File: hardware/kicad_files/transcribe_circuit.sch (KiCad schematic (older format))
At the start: 17 parts, among them J1 RS232_SERIAL, J2 MIDI_IN, J3 MIDI_OUT, U1 ProMicro, U2 MAX232, U3 6N137, U4 usbHostMini, U5 LM1117-3.3

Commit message: works with and without usb-device connected now
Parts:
- added J?: RS232_DSUB, symbol Connector:DB9_Female_MountingHoles
- C1, C2, C3, C4: footprint (none) -> Capacitor_THT:C_Axial_L3.8mm_D2.6mm_P7.50mm_Horizontal
- D1: footprint (none) -> Diode_THT:D_A-405_P7.62mm_Horizontal
- J1, J2, J3: footprint (none) -> Connector_Audio:Jack_3.5mm_CUI_SJ1-3533NG_Horizontal_CircularHoles
- R1, R2, R3, R4: footprint (none) -> Resistor_THT:R_Axial_DIN0207_L6.3mm_D2.5mm_P10.16mm_Horizontal
- U2: footprint (none) -> Package_DIP:DIP-16_W7.62mm
- U5: footprint (none) -> Package_TO_SOT_THT:TO-220-3_Horizontal_TabDown
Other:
- note added: "A. micro-controller"
- note added: "B. rs232 serial"
- note added: "C. midi serial"
- note added: "D. usb-host shield"
- note removed: "micro-controller"
- note removed: "midi serial"
- note removed: "rs232 serial"
- note removed: "usb-host shield"
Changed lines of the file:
@@
 F 0 "U1" H 2200 3537 60  0000 C CNN
 F 1 "ProMicro" H 2200 3431 60  0000 C CNN
-F 2 "" H 2300 1450 60  0000 C CNN
+F 2 "" H 2300 1450 60  0001 C CNN
 F 3 "" H 2300 1450 60  0000 C CNN
 	1    2200 2500
@@
 F 0 "U2" H 4750 4625 50  0000 C CNN
 F 1 "MAX232" H 4850 4525 50  0000 C CNN
-F 2 "" H 5250 2300 50  0001 L CNN
+F 2 "Package_DIP:DIP-16_W7.62mm" H 5250 2300 50  0001 L CNN
 F 3 "http://www.ti.com/lit/ds/symlink/max232.pdf" H 5200 3450 50  0001 C CNN
 	1    5200 3350
@@
 F 0 "U4" H 2575 7437 60  0000 C CNN
 F 1 "usbHostMini" H 2575 7331 60  0000 C CNN
-F 2 "" H 2675 5350 60  0000 C CNN
+F 2 "" H 2675 5350 60  0001 C CNN
 F 3 "" H 2675 5350 60  0000 C CNN
 	1    2575 6400
@@
 $EndComp
 Text Notes 875  950  0    118  ~ 0
-micro-controller
+A. micro-controller
 Text Notes 4275 975  0    118  ~ 0
-rs232 serial
+B. rs232 serial
 Text Notes 1000 4525 0    118  ~ 0
-usb-host shield
+D. usb-host shield
 Text Notes 7450 1025 0    118  ~ 0
-midi serial
+C. midi serial
 $Comp
 L Isolator:6N137 U3
@@
 F 0 "R1" V 8450 2225 50  0000 C CNN
 F 1 "220" V 8550 2225 50  0000 C CNN
-F 2 "" V 8480 2225 50  0001 C CNN
+F 2 "Resistor_THT:R_Axial_DIN0207_L6.3mm_D2.5mm_P10.16mm_Horizontal" V 8480 2225 50  0001 C CNN
 F 3 "~" H 8550 2225 50  0001 C CNN
 	1    8550 2225
@@
 F 0 "R2" V 9950 2125 50  0000 C CNN
 F 1 "10k" V 10050 2125 50  0000 C CNN
-F 2 "" V 9980 2125 50  0001 C CNN
+F 2 "Resistor_THT:R_Axial_DIN0207_L6.3mm_D2.5mm_P10.16mm_Horizontal" V 9980 2125 50  0001 C CNN
 F 3 "~" H 10050 2125 50  0001 C CNN
 	1    10050 2125
@@
 F 0 "D1" V 8754 2454 50  0000 L CNN
 F 1 "1N4148" H 8700 2275 50  0000 L CNN
-F 2 "" H 8800 2375 50  0001 C CNN
+F 2 "Diode_THT:D_A-405_P7.62mm_Horizontal" H 8800 2375 50  0001 C CNN
 F 3 "~" H 8800 2375 50  0001 C CNN
 	1    8800 2375
@@
 F 0 "J2" H 7932 1975 50  0000 C CNN
 F 1 "MIDI_IN" H 7932 1884 50  0000 C CNN
-F 2 "" H 7950 1650 50  0001 C CNN
+F 2 "Connector_Audio:Jack_3.5mm_CUI_SJ1-3533NG_Horizontal_CircularHoles" H 7950 1650 50  0001 C CNN
 F 3 "~" H 7950 1650 50  0001 C CNN
 	1    7950 1650
@@
 F 0 "J3" H 8007 4525 50  0000 C CNN
 F 1 "MIDI_OUT" H 8007 4434 50  0000 C CNN
-F 2 "" H 8025 4200 50  0001 C CNN
+F 2 "Connector_Audio:Jack_3.5mm_CUI_SJ1-3533NG_Horizontal_CircularHoles" H 8025 4200 50  0001 C CNN
 F 3 "~" H 8025 4200 50  0001 C CNN
 	1    8025 4200
@@
 F 0 "R3" V 9975 4200 50  0000 C CNN
 F 1 "220" V 10075 4200 50  0000 C CNN
-F 2 "" V 10005 4200 50  0001 C CNN
+F 2 "Resistor_THT:R_Axial_DIN0207_L6.3mm_D2.5mm_P10.16mm_Horizontal" V 10005 4200 50  0001 C CNN
 F 3 "~" H 10075 4200 50  0001 C CNN
 	1    10075 4200
@@
 F 0 "R4" V 9975 4425 50  0000 C CNN
 F 1 "220" V 10075 4425 50  0000 C CNN
-F 2 "" V 10005 4425 50  0001 C CNN
+F 2 "Resistor_THT:R_Axial_DIN0207_L6.3mm_D2.5mm_P10.16mm_Horizontal" V 10005 4425 50  0001 C CNN
 F 3 "~" H 10075 4425 50  0001 C CNN
 	1    10075 4425
@@
 F 0 "C1" H 4265 2646 50  0000 L CNN
 F 1 "0.1u" H 4265 2555 50  0000 L CNN
-F 2 "" H 4188 2450 50  0001 C CNN
+F 2 "Capacitor_THT:C_Axial_L3.8mm_D2.6mm_P7.50mm_Horizontal" H 4188 2450 50  0001 C CNN
 F 3 "~" H 4150 2600 50  0001 C CNN
 	1    4150 2600
@@
 F 0 "C2" H 6365 2646 50  0000 L CNN
 F 1 "0.1u" H 6365 2555 50  0000 L CNN
-F 2 "" H 6288 2450 50  0001 C CNN
+F 2 "Capacitor_THT:C_Axial_L3.8mm_D2.6mm_P7.50mm_Horizontal" H 6288 2450 50  0001 C CNN
 F 3 "~" H 6250 2600 50  0001 C CNN
 	1    6250 2600
@@
 F 0 "C3" V 6000 2950 50  0000 C CNN
 F 1 "0.1u" V 6300 2950 50  0000 C CNN
-F 2 "" H 6188 2800 50  0001 C CNN
+F 2 "Capacitor_THT:C_Axial_L3.8mm_D2.6mm_P7.50mm_Horizontal" H 6188 2800 50  0001 C CNN
 F 3 "~" H 6150 2950 50  0001 C CNN
 	1    6150 2950
@@
 F 0 "C4" V 6150 3250 50  0000 C CNN
 F 1 "0.1u" V 6450 3250 50  0000 C CNN
-F 2 "" H 6338 3100 50  0001 C CNN
+F 2 "Capacitor_THT:C_Axial_L3.8mm_D2.6mm_P7.50mm_Horizontal" H 6338 3100 50  0001 C CNN
 F 3 "~" H 6300 3250 50  0001 C CNN
 	1    6300 3250
@@
 F 0 "J1" H 4132 1900 50  0000 C CNN
 F 1 "RS232_SERIAL" H 4025 1800 50  0000 C CNN
-F 2 "" H 4150 1575 50  0001 C CNN
+F 2 "Connector_Audio:Jack_3.5mm_CUI_SJ1-3533NG_Horizontal_CircularHoles" H 4150 1575 50  0001 C CNN
 F 3 "~" H 4150 1575 50  0001 C CNN
 	1    4150 1575
@@
 F 0 "U5" H 1300 5267 50  0000 C CNN
 F 1 "LM1117-3.3" H 1300 5176 50  0000 C CNN
-F 2 "" H 1300 5025 50  0001 C CNN
+F 2 "Package_TO_SOT_THT:TO-220-3_Horizontal_TabDown" H 1300 5025 50  0001 C CNN
 F 3 "http://www.ti.com/lit/ds/symlink/lm1117.pdf" H 1300 5025 50  0001 C CNN
 	1    1300 5025
@@
 Wire Wire Line
 	2900 1950 2950 1950
+$Comp
+L Connector:DB9_Female_MountingHoles J?
+U 1 1 5E3595C7
+P 5925 1575
+F 0 "J?" H 6105 1577 50  0000 L CNN
+F 1 "RS232_DSUB" H 6105 1486 50  0000 L CNN
+F 2 "" H 5925 1575 50  0001 C CNN
+F 3 " ~" H 5925 1575 50  0001 C CNN
+	1    5925 1575
+	1    0    0    -1
+$EndComp
 $EndSCHEMATC

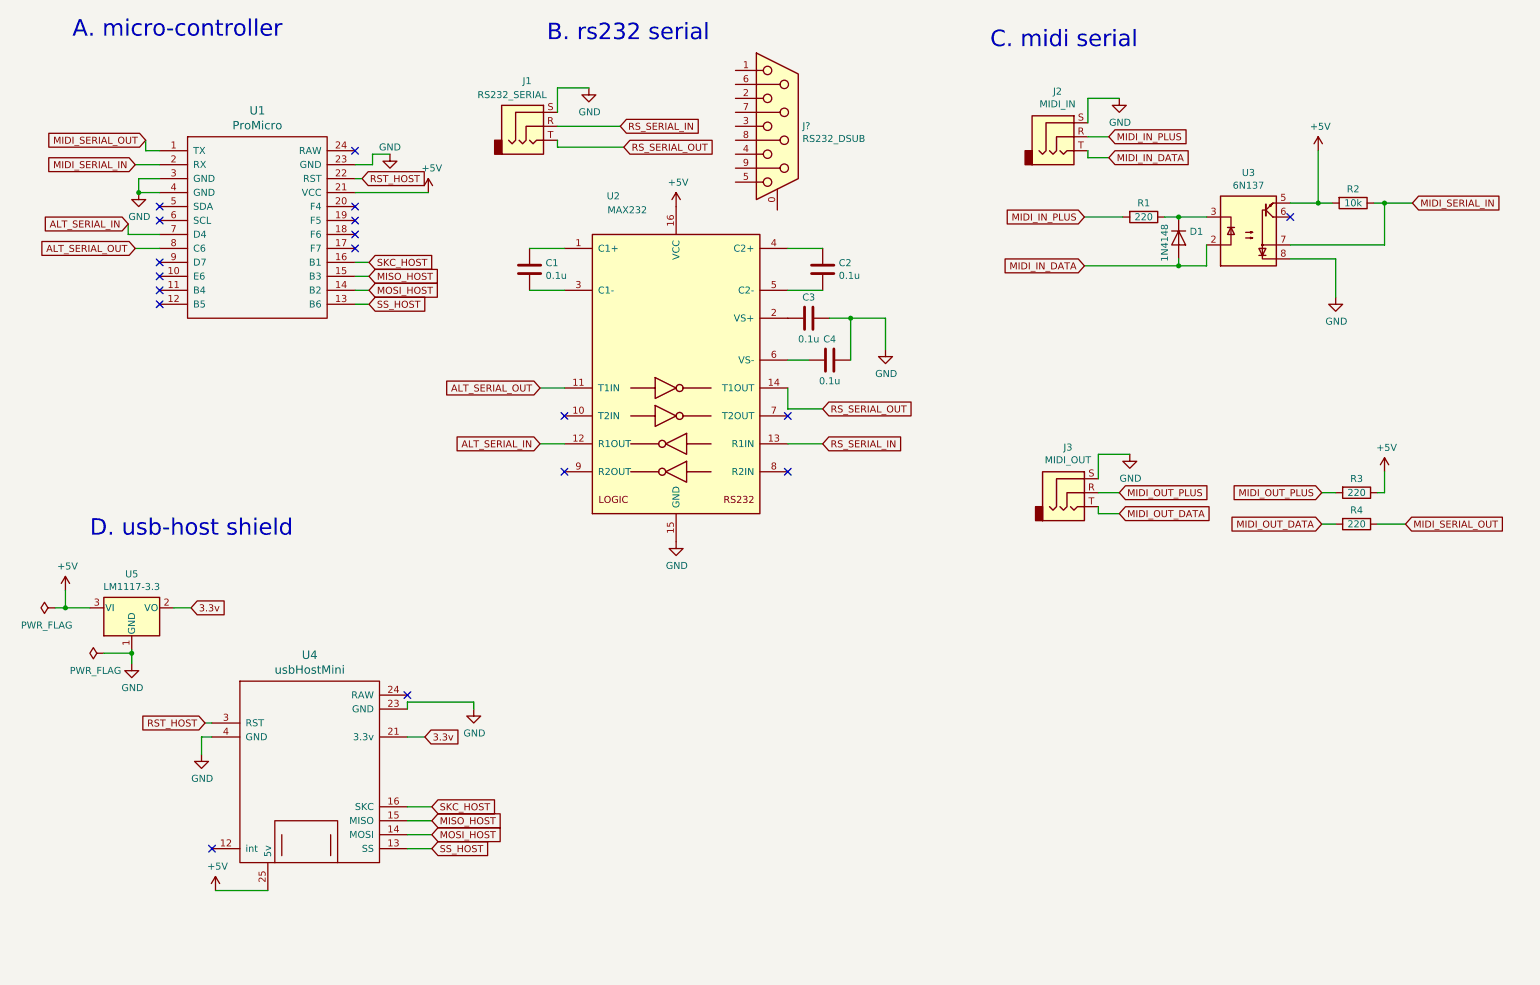
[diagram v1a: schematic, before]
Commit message: update footprints, schematic and started pcb
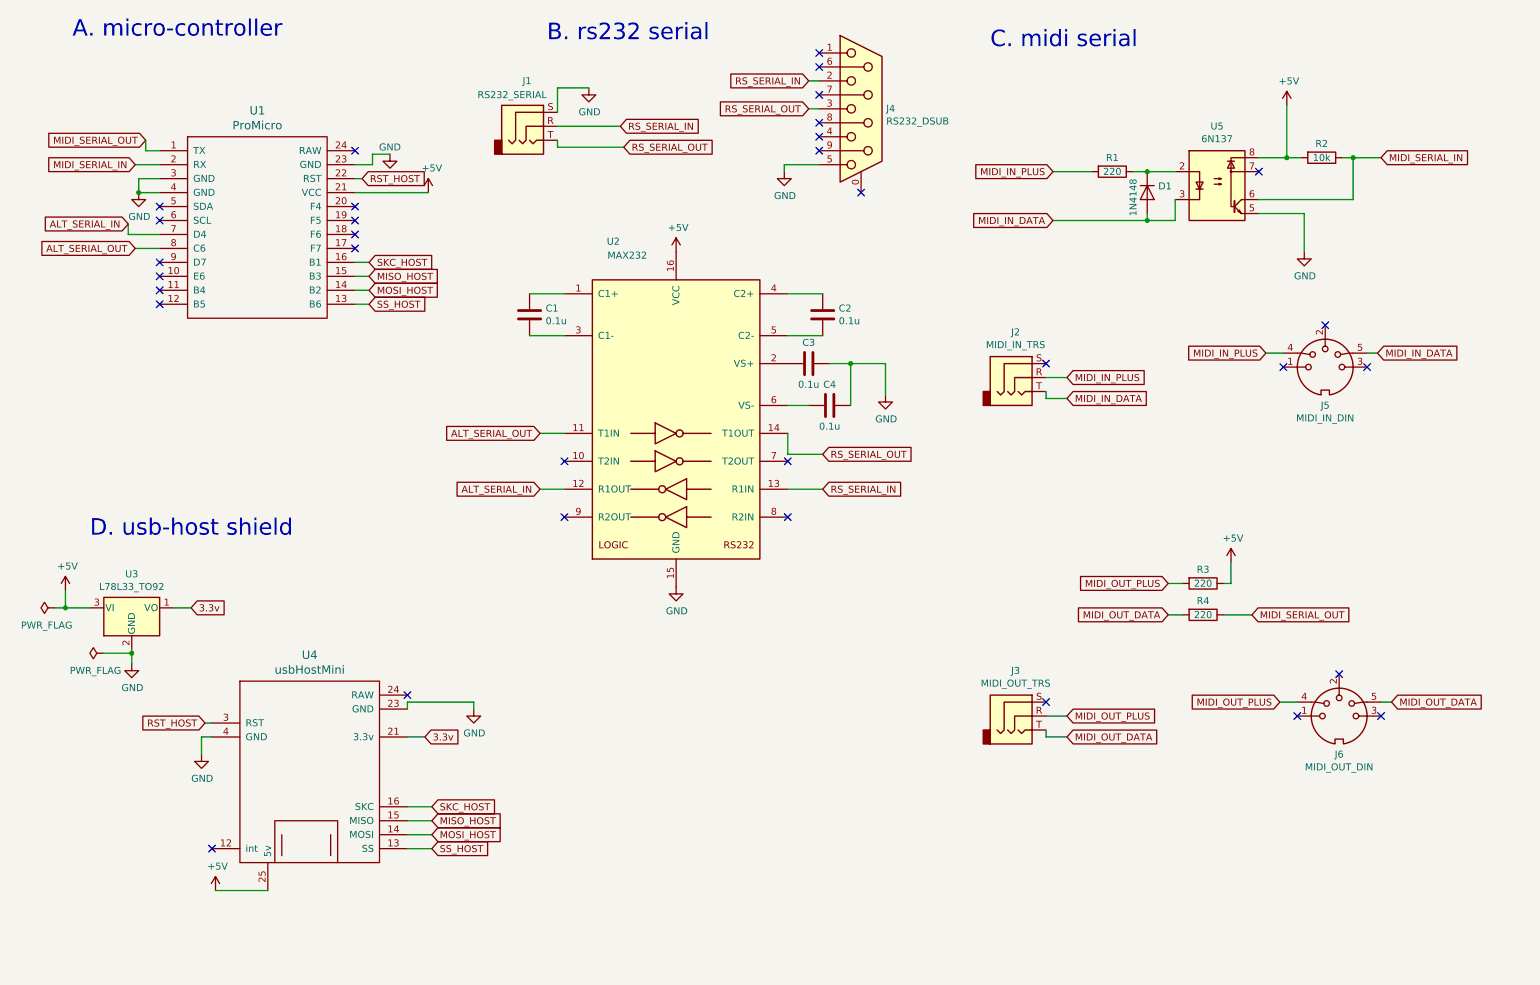
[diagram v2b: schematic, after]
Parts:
- removed U3: 6N137, Package_DIP:DIP-8_W7.62mm, symbol Isolator:6N137
- removed U5: LM1117-3.3, Package_TO_SOT_THT:TO-220-3_Horizontal_TabDown, symbol Regulator_Linear:LM1117-3.3
- added J5: MIDI_IN_DIN, Connector_DIN:SDS-50J, symbol Connector:DIN-5_180degree
- added J6: MIDI_OUT_DIN, Connector_DIN:SDS-50J, symbol Connector:DIN-5_180degree
- added U3: L78L33_TO92, Package_TO_SOT_THT:TO-92_Inline, symbol Regulator_Linear:L78L33_TO92
- added U5: 6N137, Package_DIP:DIP-8_W7.62mm, symbol Isolator:6N137
- J1: footprint Connector_Audio:Jack_3.5mm_CUI_SJ1-3533NG_Horizontal_CircularHoles -> Connector_Audio:Tayda_3.5mm_stereo_TRS_jack_A-853
- J2: value MIDI_IN -> MIDI_IN_TRS; footprint Connector_Audio:Jack_3.5mm_CUI_SJ1-3533NG_Horizontal_CircularHoles -> Connector_Audio:Tayda_3.5mm_stereo_TRS_jack_A-853
- J3: value MIDI_OUT -> MIDI_OUT_TRS; footprint Connector_Audio:Jack_3.5mm_CUI_SJ1-3533NG_Horizontal_CircularHoles -> Connector_Audio:Tayda_3.5mm_stereo_TRS_jack_A-853
- J4: renamed from J?; footprint (none) -> Connector_Dsub:DSUB-9_Female_Vertical_P2.77x2.84mm_MountingHoles
- U1: footprint (none) -> Module:ProMicro
- U4: footprint (none) -> Module:usbHostMidi
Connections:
- net +5V: now also U3.3 (VI), U5.8
- net 3.3v: now also U3.1 (VO)
- net GND: now also J4.5, U3.2 (GND), U5.5; no longer J2.S, J3.S
- net MIDI_IN_DATA: now also J5.5, U5.3
- net MIDI_IN_PLUS: now also J5.4
- net MIDI_OUT_DATA: now also J6.5
- net MIDI_OUT_PLUS: now also J6.4
- net MIDI_SERIAL_IN: now also U5.6
- net RS_SERIAL_IN: now also J4.2
- net RS_SERIAL_OUT: now also J4.3
- net at D1.1 (K), R1.1: now also U5.2
- no-connect marks 18 -> 33
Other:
- moved on the sheet: C1, C2, C3, C4, D1, J2, J3, J4, R1, R2, R3, R4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

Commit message: chipping away at pcb layout
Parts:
- C1, C2, C3, C4: footprint Capacitor_THT:C_Axial_L3.8mm_D2.6mm_P7.50mm_Horizontal -> Capacitor_THT:C_Disc_D3.0mm_W1.6mm_P2.50mm
- J5, J6: footprint Connector_DIN:SDS-50J -> Connector_DIN:Tayda5pinMidi-A1010
- R1, R2, R3, R4: footprint Resistor_THT:R_Axial_DIN0207_L6.3mm_D2.5mm_P10.16mm_Horizontal -> Resistor_THT:R_Axial_DIN0207_L6.3mm_D2.5mm_P5.08mm_Vertical
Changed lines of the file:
@@
 F 0 "R1" V 8225 1900 50  0000 C CNN
 F 1 "220" V 8325 1900 50  0000 C CNN
-F 2 "Resistor_THT:R_Axial_DIN0207_L6.3mm_D2.5mm_P10.16mm_Horizontal" V 8255 1900 50  0001 C CNN
+F 2 "Resistor_THT:R_Axial_DIN0207_L6.3mm_D2.5mm_P5.08mm_Vertical" V 8255 1900 50  0001 C CNN
 F 3 "~" H 8325 1900 50  0001 C CNN
 	1    8325 1900
@@
 F 0 "R2" V 9725 1800 50  0000 C CNN
 F 1 "10k" V 9825 1800 50  0000 C CNN
-F 2 "Resistor_THT:R_Axial_DIN0207_L6.3mm_D2.5mm_P10.16mm_Horizontal" V 9755 1800 50  0001 C CNN
+F 2 "Resistor_THT:R_Axial_DIN0207_L6.3mm_D2.5mm_P5.08mm_Vertical" V 9755 1800 50  0001 C CNN
 F 3 "~" H 9825 1800 50  0001 C CNN
 	1    9825 1800
@@
 F 0 "R3" V 8875 4850 50  0000 C CNN
 F 1 "220" V 8975 4850 50  0000 C CNN
-F 2 "Resistor_THT:R_Axial_DIN0207_L6.3mm_D2.5mm_P10.16mm_Horizontal" V 8905 4850 50  0001 C CNN
+F 2 "Resistor_THT:R_Axial_DIN0207_L6.3mm_D2.5mm_P5.08mm_Vertical" V 8905 4850 50  0001 C CNN
 F 3 "~" H 8975 4850 50  0001 C CNN
 	1    8975 4850
@@
 F 0 "R4" V 8875 5075 50  0000 C CNN
 F 1 "220" V 8975 5075 50  0000 C CNN
-F 2 "Resistor_THT:R_Axial_DIN0207_L6.3mm_D2.5mm_P10.16mm_Horizontal" V 8905 5075 50  0001 C CNN
+F 2 "Resistor_THT:R_Axial_DIN0207_L6.3mm_D2.5mm_P5.08mm_Vertical" V 8905 5075 50  0001 C CNN
 F 3 "~" H 8975 5075 50  0001 C CNN
 	1    8975 5075
@@
 F 0 "C1" H 4265 2971 50  0000 L CNN
 F 1 "0.1u" H 4265 2880 50  0000 L CNN
-F 2 "Capacitor_THT:C_Axial_L3.8mm_D2.6mm_P7.50mm_Horizontal" H 4188 2775 50  0001 C CNN
+F 2 "Capacitor_THT:C_Disc_D3.0mm_W1.6mm_P2.50mm" H 4188 2775 50  0001 C CNN
 F 3 "~" H 4150 2925 50  0001 C CNN
 	1    4150 2925
@@
 F 0 "C2" H 6365 2971 50  0000 L CNN
 F 1 "0.1u" H 6365 2880 50  0000 L CNN
-F 2 "Capacitor_THT:C_Axial_L3.8mm_D2.6mm_P7.50mm_Horizontal" H 6288 2775 50  0001 C CNN
+F 2 "Capacitor_THT:C_Disc_D3.0mm_W1.6mm_P2.50mm" H 6288 2775 50  0001 C CNN
 F 3 "~" H 6250 2925 50  0001 C CNN
 	1    6250 2925
@@
 F 0 "C3" V 6000 3275 50  0000 C CNN
 F 1 "0.1u" V 6300 3275 50  0000 C CNN
-F 2 "Capacitor_THT:C_Axial_L3.8mm_D2.6mm_P7.50mm_Horizontal" H 6188 3125 50  0001 C CNN
+F 2 "Capacitor_THT:C_Disc_D3.0mm_W1.6mm_P2.50mm" H 6188 3125 50  0001 C CNN
 F 3 "~" H 6150 3275 50  0001 C CNN
 	1    6150 3275
@@
 F 0 "C4" V 6150 3575 50  0000 C CNN
 F 1 "0.1u" V 6450 3575 50  0000 C CNN
-F 2 "Capacitor_THT:C_Axial_L3.8mm_D2.6mm_P7.50mm_Horizontal" H 6338 3425 50  0001 C CNN
+F 2 "Capacitor_THT:C_Disc_D3.0mm_W1.6mm_P2.50mm" H 6338 3425 50  0001 C CNN
 F 3 "~" H 6300 3575 50  0001 C CNN
 	1    6300 3575
@@
 F 0 "J6" H 9950 5525 50  0000 C CNN
 F 1 "MIDI_OUT_DIN" H 9950 5434 50  0000 C CNN
-F 2 "Connector_DIN:SDS-50J" H 9950 5800 50  0001 C CNN
+F 2 "Connector_DIN:Tayda5pinMidi-A1010" H 9950 5800 50  0001 C CNN
 F 3 "http://www.mouser.com/ds/2/18/40_c091_abd_e-75918.pdf" H 9950 5800 50  0001 C CNN
 	1    9950 5800
@@
 F 0 "J5" H 9850 3025 50  0000 C CNN
 F 1 "MIDI_IN_DIN" H 9850 2934 50  0000 C CNN
-F 2 "Connector_DIN:SDS-50J" H 9850 3300 50  0001 C CNN
+F 2 "Connector_DIN:Tayda5pinMidi-A1010" H 9850 3300 50  0001 C CNN
 F 3 "http://www.mouser.com/ds/2/18/40_c091_abd_e-75918.pdf" H 9850 3300 50  0001 C CNN
 	1    9850 3300

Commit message: wip
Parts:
- added C1: 100uf, Capacitor_THT:CP_Radial_D6.3mm_P2.50mm, symbol Device:CP
- added J1: europower, Connector_PinHeader_2.54mm:PinHeader_2x08_P2.54mm_Vertical, symbol Connector_Generic:Conn_02x08_Odd_Even
- added U4: 4069, Package_DIP:DIP-14_W7.62mm, symbol 4xxx:4069
- J2: renamed from J1; symbol Connector:AudioJack3 -> Connector:AudioJack3_SwitchTR
- J4: renamed from J2; symbol Connector:AudioJack3 -> Connector:AudioJack3_SwitchTR
- J6: renamed from J3; symbol Connector:AudioJack3 -> Connector:AudioJack3_SwitchTR
- renumbered C1 to C2, C2 to C4, C4 to C5, J4 to J3, J6 to J7, R3 to R1, R4 to R2, R1 to R3, R2 to R4, U5 to U3, U4 to U5, U3 to U6
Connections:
- net +5V: now also U1.24 (RAW), C1.1, J1.11 (Pin_11), J1.12 (Pin_12), U4.14 (VDD); no longer U1.21 (VCC)
- net GND: now also J2.RN, J2.TN, J3.0 (PAD), C1.2, J1.3 (Pin_3), J1.4 (Pin_4), J1.5 (Pin_5), J1.6 (Pin_6), J1.7 (Pin_7), J1.8 (Pin_8), U4.7 (VSS)
- net MIDI_SERIAL_OUT: now also U4.3; no longer R2.1
- new net: R2.1, U4.2
- new net: U4.1, U4.4
- no-connect marks 33 -> 52
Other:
- moved on the sheet: R1, R2
